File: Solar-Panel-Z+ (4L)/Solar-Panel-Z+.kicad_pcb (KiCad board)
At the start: 4 copper layers, 48.4 x 48.4 mm, 79 parts, among them J1 FTS-105-01-L-DV-A, Q1 BSS138DWQ-7, Q2 MBT2222ADW1T1, Q3 BSS138DWQ-7, Q4 MBT2222ADW1T1, U1 BQ25570RGRR, U2 TSL2561

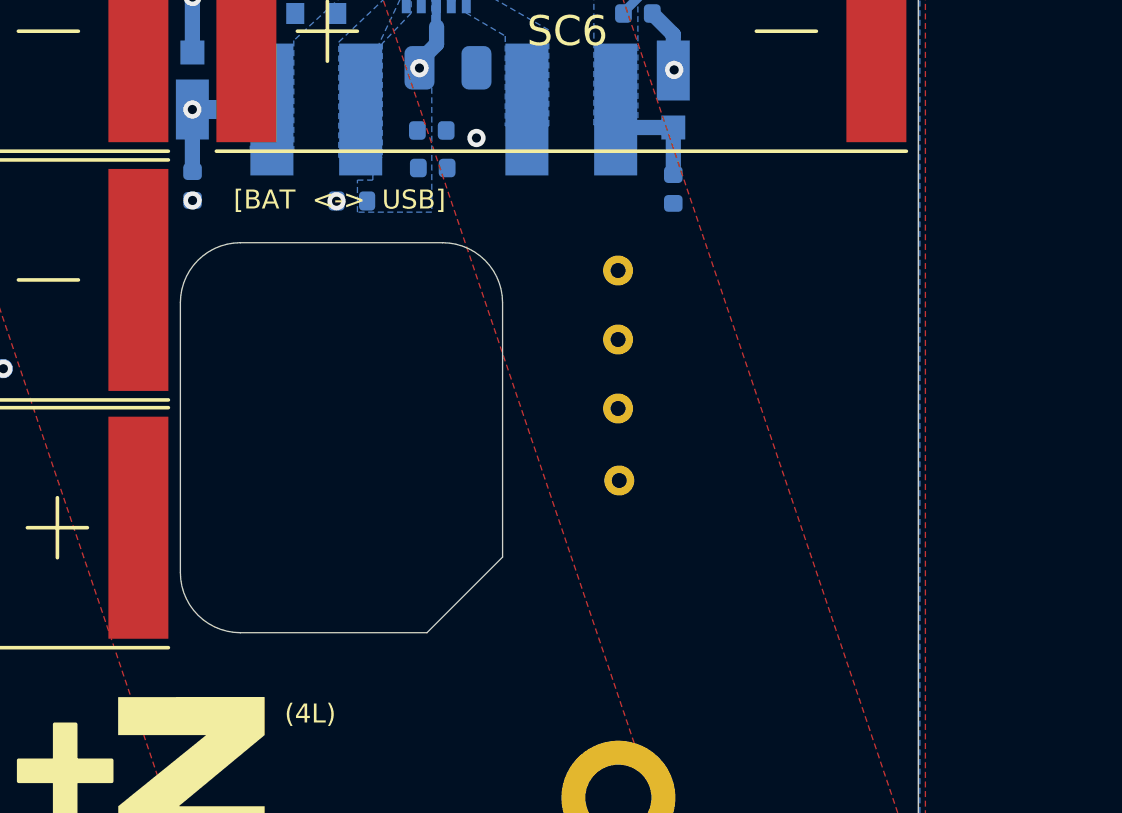
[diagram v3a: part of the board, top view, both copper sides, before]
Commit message: Moved Access Port for new USBC location
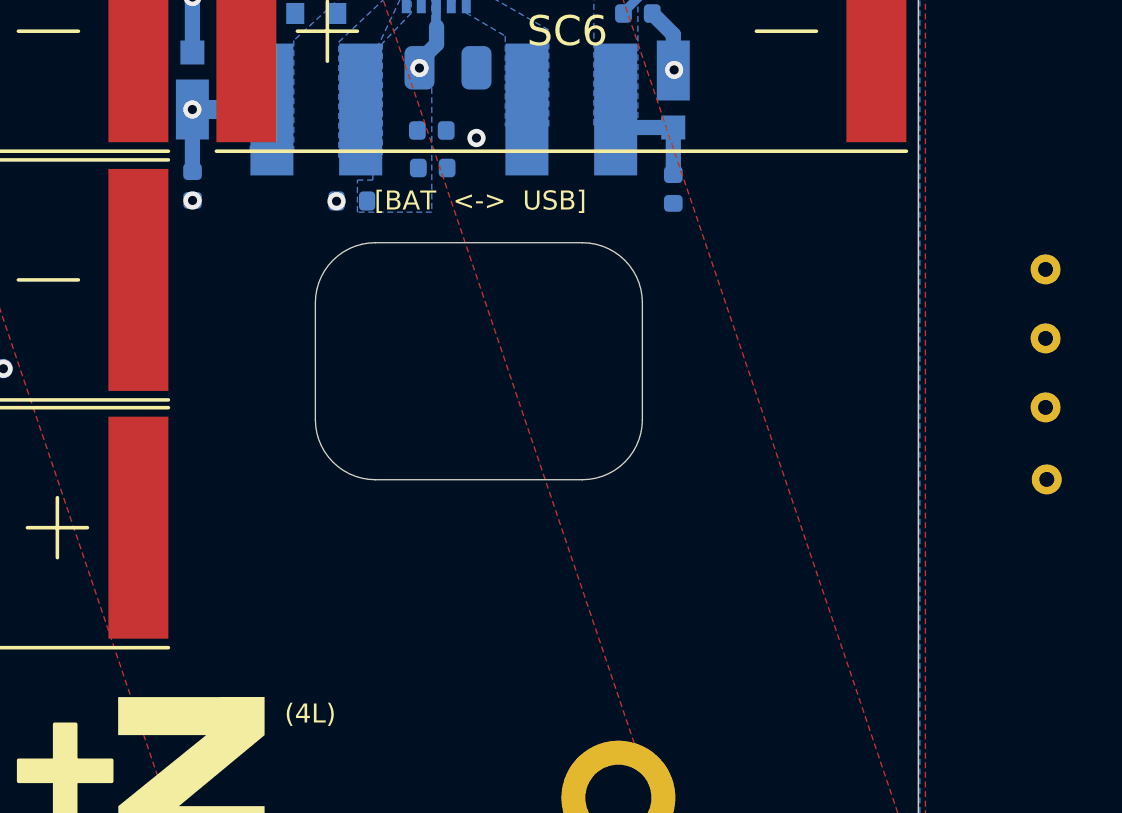
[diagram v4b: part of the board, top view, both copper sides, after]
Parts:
- moved TP1 14.3 mm to (135.2, 77.1)
- moved TP2 14.3 mm to (135.1, 74.7)
- moved TP3 14.3 mm to (135.1, 70.1)
- moved TP4 14.3 mm to (135.1, 72.4)
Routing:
- net VSOLAR: track 30.2 -> 6.11 mm
- net VBAT: track 43.9 -> 30.2 mm
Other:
- outline, holes or cut-outs redrawn
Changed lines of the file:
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@@
   )
   (footprint "TestPoint:TestPoint_THTPad_D1.0mm_Drill0.5mm" (layer "B.Cu")
-    (at 120.8894 74.7268 180)
+    (at 135.14 74.69 180)
     (descr "THT pad as test Point, diameter 1.0mm, hole diameter 0.5mm")
     (tags "test point THT pad")
@@
   )
   (footprint "TestPoint:TestPoint_THTPad_D1.0mm_Drill0.5mm" (layer "B.Cu")
-    (at 120.8894 70.1268)
+    (at 135.14 70.09)
     (descr "THT pad as test Point, diameter 1.0mm, hole diameter 0.5mm")
     (tags "test point THT pad")
@@
   )
   (footprint "TestPoint:TestPoint_THTPad_D1.0mm_Drill0.5mm" (layer "B.Cu")
-    (at 120.8894 72.4268)
+    (at 135.14 72.39)
     (descr "THT pad as test Point, diameter 1.0mm, hole diameter 0.5mm")
     (tags "test point THT pad")
@@
   )
   (footprint "TestPoint:TestPoint_THTPad_D1.0mm_Drill0.5mm" (layer "B.Cu")
-    (at 120.9294 77.1268 180)
+    (at 135.18 77.09 180)
     (descr "THT pad as test Point, diameter 1.0mm, hole diameter 0.5mm")
     (tags "test point THT pad")
@@
   (gr_line (start 108.361 52.4) (end 108.0435 52.4) (layer "B.SilkS") (width 0.12))
   (gr_line (start 105.02725 52.4) (end 105.34475 52.4) (layer "B.SilkS") (width 0.12))
-  (gr_line (start 123.9 78.7) (end 117.1 78.7) (layer "B.SilkS") (width 0.0254))
+  (gr_line (start 123.9 78.7) (end 106.275 78.7) (layer "B.SilkS") (width 0.0254))
   (gr_line (start 91.1 78.7) (end 106.275 78.7) (layer "B.SilkS") (width 0.0254))
   (gr_line (start 123.9 48.3) (end 91.1 48.3) (layer "B.SilkS") (width 0.0254))
@@
   (gr_line (start 82.5 90.7) (end 82.5 42.3) (layer "Edge.Cuts") (width 0.05))
   (gr_line (start 82.5 42.3) (end 130.9 42.3) (layer "Edge.Cuts") (width 0.05))
-  (gr_line (start 115.04 69.2) (end 108.3 69.2) (layer "Edge.Cuts") (width 0.0254))
-  (gr_line (start 117.04 79.68) (end 117.04 71.2) (layer "Edge.Cuts") (width 0.0254))
+  (gr_line (start 119.7 77.1) (end 112.8 77.1) (layer "Edge.Cuts") (width 0.0254))
+  (gr_line (start 119.7 69.2) (end 112.8 69.2) (layer "Edge.Cuts") (width 0.0254))
+  (gr_line (start 121.7 75.1) (end 121.7 71.2) (layer "Edge.Cuts") (width 0.0254))
+  (gr_arc (start 121.7 75.1) (mid 121.114214 76.514214) (end 119.7 77.1) (layer "Edge.Cuts") (width 0.0254))
   (gr_line (start 82.5 90.7) (end 130.9 90.7) (layer "Edge.Cuts") (width 0.05))
-  (gr_arc (start 106.3 71.2) (mid 106.885786 69.785786) (end 108.3 69.2) (layer "Edge.Cuts") (width 0.0254))
-  (gr_arc (start 115.04 69.2) (mid 116.454214 69.785786) (end 117.04 71.2) (layer "Edge.Cuts") (width 0.0254))
-  (gr_arc (start 108.3 82.2) (mid 106.885786 81.614214) (end 106.3 80.2) (layer "Edge.Cuts") (width 0.0254))
+  (gr_arc (start 110.8 71.2) (mid 111.385786 69.785786) (end 112.8 69.2) (layer "Edge.Cuts") (width 0.0254))
+  (gr_arc (start 119.7 69.2) (mid 121.114214 69.785786) (end 121.7 71.2) (layer "Edge.Cuts") (width 0.0254))
+  (gr_arc (start 112.8 77.1) (mid 111.385786 76.514214) (end 110.8 75.1) (layer "Edge.Cuts") (width 0.0254))
   (gr_line (start 130.9 42.3) (end 130.9 90.7) (layer "Edge.Cuts") (width 0.05))
-  (gr_line (start 106.3 71.2) (end 106.3 80.2) (layer "Edge.Cuts") (width 0.0254))
-  (gr_line (start 108.3 82.2) (end 114.52 82.2) (layer "Edge.Cuts") (width 0.0254))
-  (gr_line (start 114.52 82.2) (end 117.04 79.68) (layer "Edge.Cuts") (width 0.0254))
-  (gr_text "GND" (at 120.0658 74.7014) (layer "B.SilkS")
+  (gr_line (start 110.8 71.2) (end 110.8 75.1) (layer "Edge.Cuts") (width 0.0254))
+  (gr_text "GND" (at 143.2508 74.667) (layer "B.SilkS")
     (effects (font (size 0.508 0.508) (thickness 0.0762)) (justify left mirror))
   )
-  (gr_text "VSOLAR" (at 120.015 77.1144) (layer "B.SilkS")
+  (gr_text "VSOLAR" (at 143.2 77.08) (layer "B.SilkS")
     (effects (font (size 0.508 0.508) (thickness 0.0762)) (justify left mirror))
   )
-  (gr_text "VBAT" (at 120.015 72.4) (layer "B.SilkS")
+  (gr_text "VBAT" (at 143.2 72.3656) (layer "B.SilkS")
     (effects (font (size 0.508 0.508) (thickness 0.0762)) (justify left mirror))
   )
-  (gr_text "3V3" (at 120.0404 70.1548) (layer "B.SilkS")
+  (gr_text "3V3" (at 143.2254 70.1204) (layer "B.SilkS")
     (effects (font (size 0.508 0.508) (thickness 0.0762)) (justify left mirror))
   )
@@
     (effects (font (size 0.889 0.889) (thickness 0.15)))
   )
-  (gr_text "[BAT  <->  USB]" (at 111.6076 67.7672) (layer "F.SilkS")
+  (gr_text "[BAT  <->  USB]" (at 116.3 67.8) (layer "F.SilkS")
     (effects (font (size 0.635 0.635) (thickness 0.1016)))
   )
@@
     (pts (xy 82.5 42.3) (xy 82.5 90.7))
     (height 2.1)
-    (gr_text "1905.5118 mils" (at 79.25 66.5 90) (layer "Dwgs.User")
+    (gr_text "48.4000 mm" (at 79.25 66.5 90) (layer "Dwgs.User")
       (effects (font (size 1 1) (thickness 0.15)))
     )
@@
     (pts (xy 82.5 42.3) (xy 130.9 42.3))
     (height -2.1)
-    (gr_text "1905.5118 mils" (at 106.7 39.05) (layer "Dwgs.User")
+    (gr_text "48.4000 mm" (at 106.7 39.05) (layer "Dwgs.User")
       (effects (font (size 1 1) (thickness 0.15)))
     )
@@
   (segment (start 120.02924 59.46) (end 119.031784 59.46) (width 0.254) (layer "B.Cu") (net 5))
   (via (at 106.7 64.76) (size 0.6096) (drill 0.3048) (layers "F.Cu" "B.Cu") (net 6))
-  (segment (start 116.72 64.76) (end 118.31 66.35) (width 0.508) (layer "In1.Cu") (net 6))
-  (segment (start 118.31 66.35) (end 118.31 74.5074) (width 0.508) (layer "In1.Cu") (net 6))
-  (segment (start 106.7 64.76) (end 116.72 64.76) (width 0.508) (layer "In1.Cu") (net 6))
-  (segment (start 118.31 74.5074) (end 120.9294 77.1268) (width 0.508) (layer "In1.Cu") (net 6))
   (segment (start 111.36079 60.03079) (end 110.37079 59.04079) (width 0.254) (layer "B.Cu") (net 6))
   (segment (start 106.7 64.76) (end 106.7 66.8246) (width 0.508) (layer "B.Cu") (net 6))
@@
   (via (at 92.65 70.95) (size 0.6096) (drill 0.3048) (layers "F.Cu" "B.Cu") (net 40))
   (via (at 114.27 63.38) (size 0.6096) (drill 0.3048) (layers "F.Cu" "B.Cu") (net 40))
-  (segment (start 119.8 71.3374) (end 120.8894 72.4268) (width 0.508) (layer "In1.Cu") (net 40))
   (segment (start 92.65 67.72) (end 96.99 63.38) (width 0.508) (layer "In1.Cu") (net 40))
   (segment (start 96.99 63.38) (end 114.27 63.38) (width 0.508) (layer "In1.Cu") (net 40))
   (segment (start 92.65 70.95) (end 92.65 67.72) (width 0.508) (layer "In1.Cu") (net 40))
-  (segment (start 119.8 65.6472) (end 119.8 71.3374) (width 0.508) (layer "In1.Cu") (net 40))
-  (segment (start 114.27 63.38) (end 117.5328 63.38) (width 0.508) (layer "In1.Cu") (net 40))
-  (segment (start 117.5328 63.38) (end 119.8 65.6472) (width 0.508) (layer "In1.Cu") (net 40))
   (segment (start 92.65 70.95) (end 92.65 72.29) (width 0.508) (layer "B.Cu") (net 40))
   (segment (start 114.84 62.58) (end 114.84 62) (width 0.508) (layer "B.Cu") (net 40))

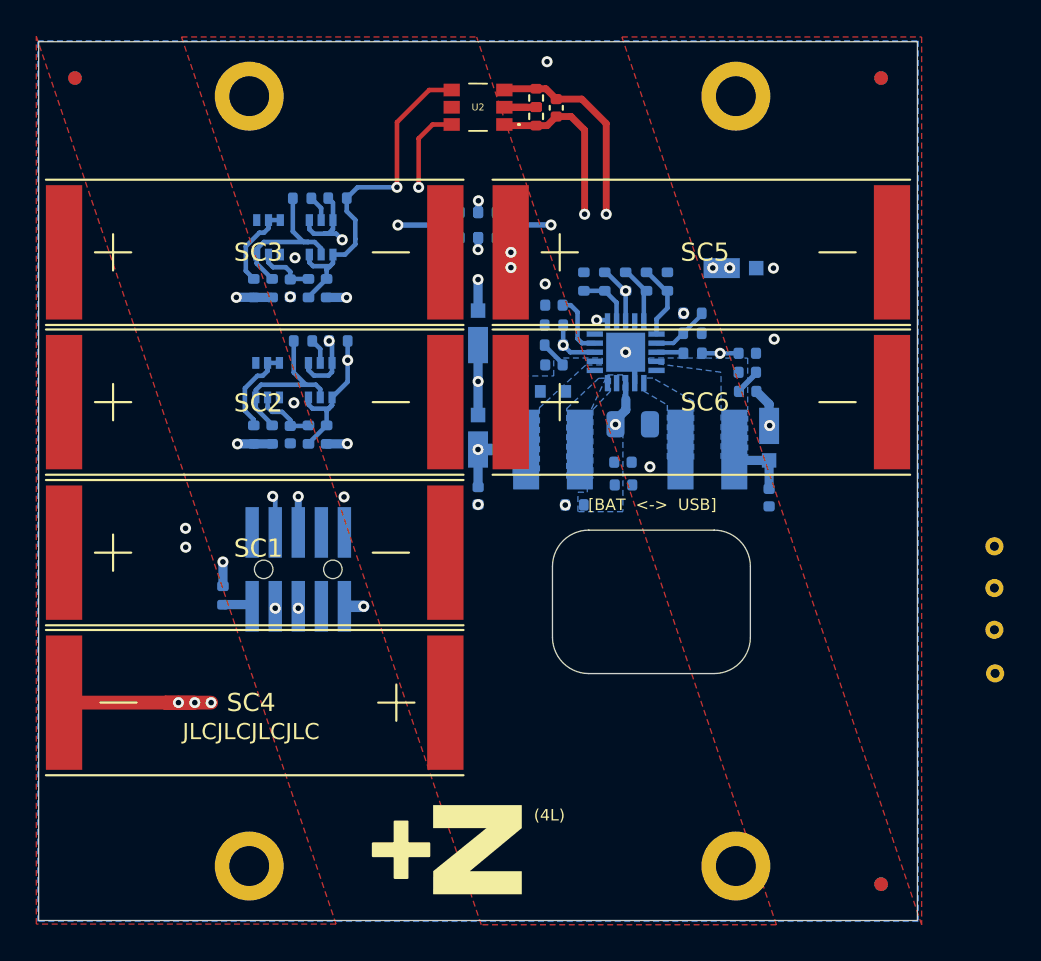
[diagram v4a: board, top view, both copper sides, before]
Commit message: Updated all solar panels to Rev B2/01 + Export STEP / BOM
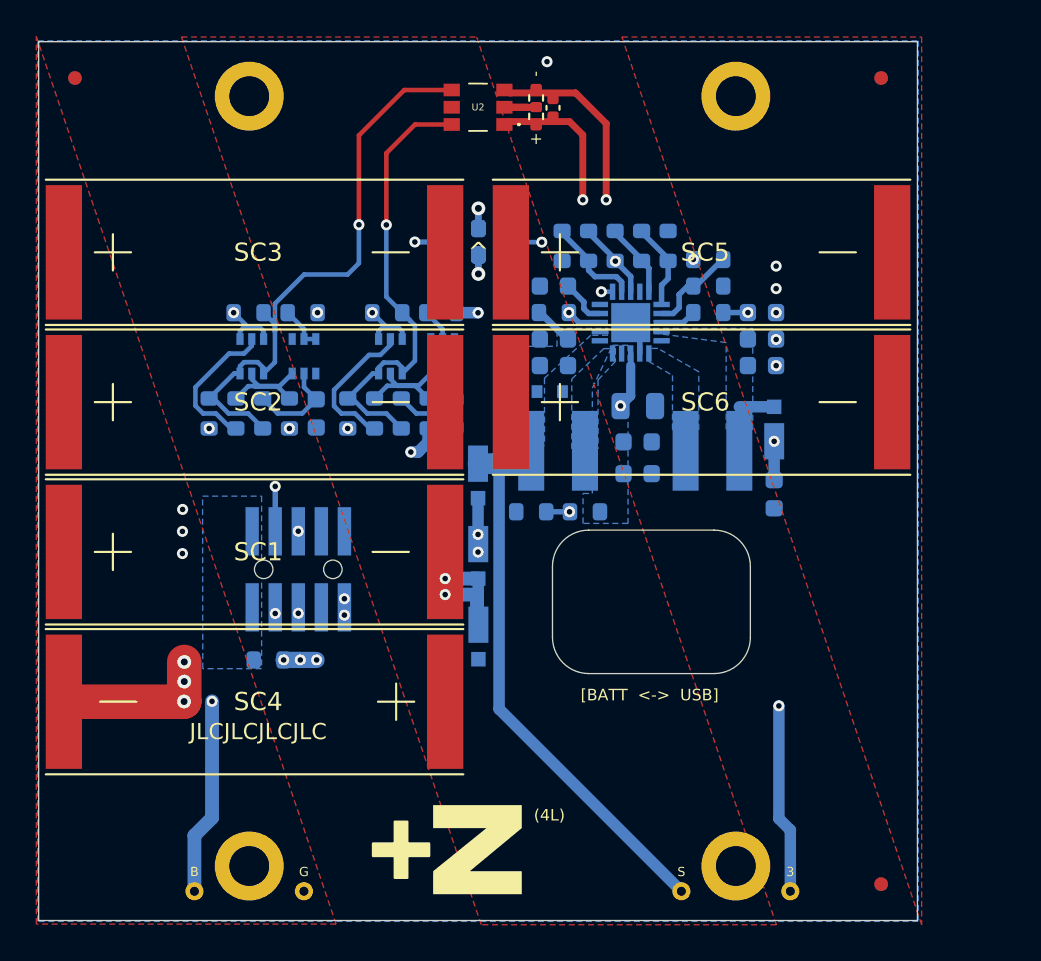
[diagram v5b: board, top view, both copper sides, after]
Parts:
- removed the Ref** at (100.0, 85.1)
- added Ref**: Val**, custom-footprints:pycubed_mini_half, B.Cu at (106.2, 44.6)
- C10, C11, C12, C13, C2, C3, C4, C6, C7, C8, C9: footprint Capacitor_SMD:C_0402_1005Metric -> Capacitor_SMD:C_0603_1608Metric
- J1: footprint batteryboard:FTS-105-XX-YY-DV-A -> solarpanels:SAMTEC-FTS-105-01-X-DV-A
- R10, R11, R12, R13, R16, R17, R18, R3, R5, R6, R7, R8, R9: footprint Resistor_SMD:R_0402_1005Metric -> Resistor_SMD:R_0603_1608Metric
- R14, R15: value 0 -> DNI; footprint Resistor_SMD:R_0402_1005Metric -> Resistor_SMD:R_0603_1608Metric
- R19: renamed from R22; value 0 -> DNI; footprint Resistor_SMD:R_0402_1005Metric -> Resistor_SMD:R_0603_1608Metric
- R20: renamed from R23; value 0 -> DNI; footprint Resistor_SMD:R_0402_1005Metric -> Resistor_SMD:R_0603_1608Metric
- R21: renamed from R20; footprint Resistor_SMD:R_0402_1005Metric -> Resistor_SMD:R_0603_1608Metric
- R22: renamed from R21; footprint Resistor_SMD:R_0402_1005Metric -> Resistor_SMD:R_0603_1608Metric
- R23: renamed from R24; footprint Resistor_SMD:R_0402_1005Metric -> Resistor_SMD:R_0603_1608Metric
- R24: renamed from R25; footprint Resistor_SMD:R_0402_1005Metric -> Resistor_SMD:R_0603_1608Metric
- R25: renamed from R26; footprint Resistor_SMD:R_0402_1005Metric -> Resistor_SMD:R_0603_1608Metric
- R26: renamed from R27; footprint Resistor_SMD:R_0402_1005Metric -> Resistor_SMD:R_0603_1608Metric
- R27: renamed from R28; footprint Resistor_SMD:R_0402_1005Metric -> Resistor_SMD:R_0603_1608Metric
- R28: renamed from R29; footprint Resistor_SMD:R_0402_1005Metric -> Resistor_SMD:R_0603_1608Metric
- R29: renamed from R30; footprint Resistor_SMD:R_0402_1005Metric -> Resistor_SMD:R_0603_1608Metric
- R30: renamed from R31; footprint Resistor_SMD:R_0402_1005Metric -> Resistor_SMD:R_0603_1608Metric
- R4: renamed from R19; footprint Resistor_SMD:R_0402_1005Metric -> Resistor_SMD:R_0603_1608Metric
- moved TP4 47.1 mm to (91.1, 89.1)
- moved TP2 40.7 mm to (97.1, 89.1)
- moved D3 24.7 mm to (106.7, 75.1), turned to -90 degrees
- moved TP3 22.1 mm to (123.9, 89.1)
- moved TP1 21.0 mm to (117.9, 89.1)
- moved R21 12.4 mm to (93.4, 62.8), turned to 90 degrees
- moved R27 12.3 mm to (104.7, 57.2), turned to 180 degrees
- moved D4 12.3 mm to (106.7, 70.6), turned to -90 degrees
- moved R15 10.4 mm to (109.6, 68.2)
- moved Q3 9.73 mm to (104.8, 59.6)
- moved R24 9.46 mm to (91.9, 62.8)
- moved C13 9.14 mm to (105.4, 62.8)
- moved R28 8.67 mm to (104.0, 62.8)
- moved C2 8.30 mm to (110.9, 60.1), turned to 0 degrees
- moved R19 7.99 mm to (94.1, 57.2)
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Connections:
- net SCL2 renamed SCL
- net SDA2 renamed SDA
- J1 pad 10: VUSB -> BATT_P
- J1 pad 4: BURN2 -> GND
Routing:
- net VSOLAR: track 6.11 -> 32.7 mm, vias 1 -> 0
- net VBAT: track 30.2 -> 16.9 mm, vias 2 -> 5
- net SCL_LS: track 19.1 -> 32.0 mm
- net Net-(D3-Pad1): track 14.6 -> 6.71 mm, vias 5 -> 2
- net Net-(Q2-Pad2): track 1.42 -> 7.92 mm
- net Net-(Q4-Pad2): track 1.39 -> 7.84 mm
- net SCL: track 22.7 -> 16.9 mm
- net +3V3: track 19.0 -> 23.8 mm, vias 7 -> 11
- net SDA: track 19.6 -> 24.0 mm
- net /coil: track 6598.4 -> 6601.7 mm
- net GND: track 23.5 -> 20.5 mm, vias 14 -> 9
- net Net-(Q3-Pad2): track 4.98 -> 2.47 mm
- net Net-(Q3-Pad6): track 9.19 -> 6.72 mm
- net Net-(Q1-Pad6): track 9.10 -> 6.70 mm
- net Net-(Q1-Pad2): track 4.74 -> 2.47 mm
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- added copper zone on In2.Cu, net +3V3
- added copper zone on B.Cu, net BATT_P
- added copper zone on In1.Cu, net VBAT
- removed copper zone on In1.Cu, net +3V3
- removed copper zone on In2.Cu, net GND
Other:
- board text added: "1.3V3 3.BURN1 5.COIL_P 7.SDA 9.BATT_P"
- board text added: "2.GND 4.GND 6.COIL_N 8.SCL 10.BATT_P"
- board text added: "3"
- board text added: "B"
- board text added: "G"
- board text added: "Rev B2/01"
- board text added: "S"
- board text added: "[BATT <-> USB]"
- board text added: "^"
- board text added: "⊗"
- board text added: "⊙"
- board text removed: "08-AUG-2022"
- board text removed: "Cable Pinout 1.BATT_P 2.VUSB 3.BURN1 4.BURN2 5.COIL_P 6.COIL_N 7.SDA 8.SCL 9.+3V3 10.GND"
- board text removed: "[BAT <-> USB]"
- board text removed: "v04"
